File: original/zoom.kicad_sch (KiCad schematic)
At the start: 161 parts, among them U10 1NB4-5040, U11 1NB4-5040, U12 1NB4-5040, U14 1821-4731, U2 LM2991, U7 LT1086-CM, U77 74LVC08, U78 74LVC08, U8 1NB4-5040, U9 1NB4-5040

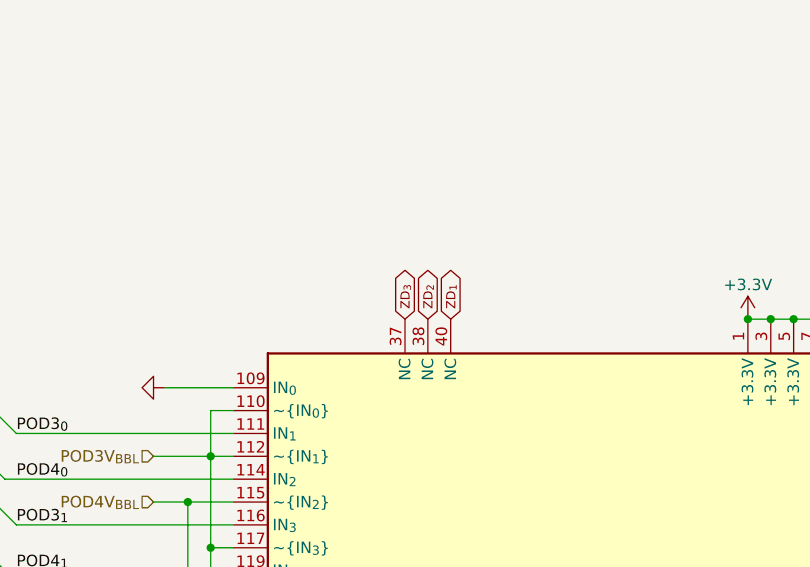
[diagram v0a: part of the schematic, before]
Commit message: fix original version ECL routing to ASICs
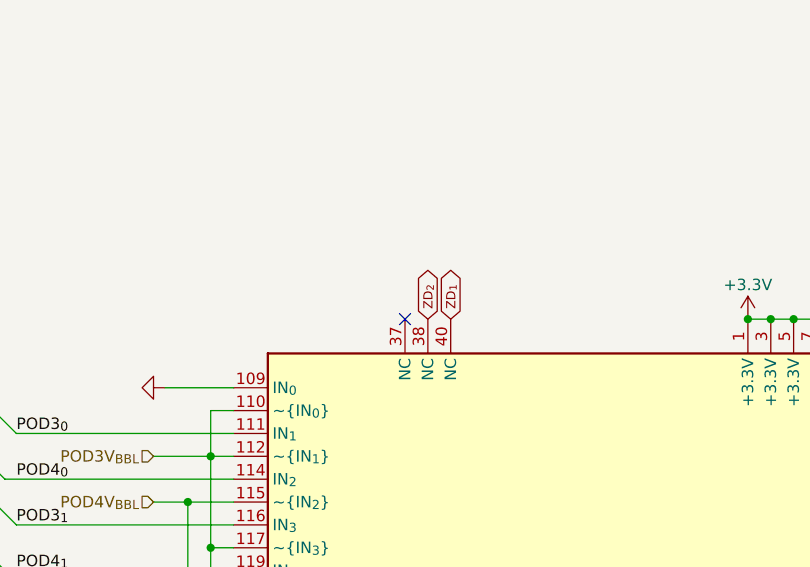
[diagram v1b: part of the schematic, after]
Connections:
- net ZD_{3}: no longer U12.37 (NC)
- no-connect marks 31 -> 32
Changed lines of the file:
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@@
 	)
 	(no_connect
+		(at 214.63 81.28)
+	)
+	(no_connect
 		(at 318.77 219.71)
 	)
@@
 			(effects
 				(font
-					(size 1.27 1.27)
-				)
-				(justify left)
-				(hide yes)
-			)
-		)
-	)
-	(global_label "ZD_{3}"
-		(shape bidirectional)
-		(at 214.63 81.28 90)
-		(fields_autoplaced yes)
-		(effects
-			(font
-				(size 1.016 1.016)
-			)
-			(justify left)
-		)
-		(property "Intersheetrefs" "${INTERSHEET_REFS}"
-			(at 214.63 75.2048 90)
-			(effects
-				(font

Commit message: clean up routing & add test points on original design
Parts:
- removed C1081, C1085, C1291, C1305, C1321, C1327: 100p, fp:C0603, symbol Device:C_Small
- added TP1087, TP1088, TP121, TP122, TP123, TP124, TP125, TP126, TP127, TP128, TP370, TP547, TP548, TP549, TP554, TP613, TP652, TP653, TP654, TP655, TP656, TP657, TP658, TP659, TP661, TP78, TP784, TP79, TP80, TP816, TP817, TP818, TP819, TP820, TP821, TP822, TP823, TP824, TP825, TP826, TP827, TP828, TP830, TP832, TP833, TP834, TP835, TP836, TP856, TP857, TP858, TP859, TP860, TP861, TP862, TP863, TP864, TP867, TP868, TP869, TP870, TP871, TP872, TP874, TP880, TP881, TP882, TP883, TP884, TP885, TP886, TP887, TP888, TP889, TP890, TP891, TP892, TP893, TP894, TP895, TP896: ~, fp:TestPoint, symbol 16717a:TestPoint_Small
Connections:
- net +3.3V: now also TP816.1, TP818.1, TP819.1, TP821.1, TP823.1, TP825.1, TP826.1, TP828.1, TP830.1, TP833.1, TP834.1, TP856.1, TP857.1, TP880.1, TP896.1
- net +3.3VP: now also TP1087.1, TP1088.1, TP549.1; no longer U2.2 (~{ON}/OFF)
- net -1.7V: now also TP79.1
- net -3.3V: now also TP548.1
- net CLKA_{0}-: now also TP653.1
- net CLKA_{1}-: now also TP655.1
- net CLKA_{2}-: now also TP657.1
- net CLKA_{3}-: now also TP659.1
- net CLKA_{4}+: now also TP661.1
- net CLKB_{0}+: now also TP652.1
- net CLKB_{1}+: now also TP654.1
- net CLKB_{2}+: now also TP656.1
- net CLKB_{3}+: now also TP658.1
- net GND: now also TP554.1, TP613.1, TP78.1, TP784.1, TP80.1, TP817.1, TP820.1, TP822.1, TP824.1, TP827.1, TP832.1, TP835.1, TP836.1, TP859.1, TP860.1, TP861.1, TP862.1, TP863.1, TP864.1, TP874.1; no longer U78.10, U78.12, U78.13, U78.4, U78.5, U78.9
- net POD1V_{BB}_{H}: now also TP867.1
- net POD1_{4}: now also TP370.1
- net POD2V_{BB}_{H}: now also TP872.1
- net POD2V_{BB}_{L}: now also TP868.1
- net POD3V_{BB}_{H}: now also TP869.1
- net POD4V_{BB}_{H}: now also TP871.1
- net POD4V_{BB}_{L}: now also TP870.1
- net ZD_{0}: now also TP121.1
- net ZD_{1}: now also TP122.1
- net ZD_{2}: now also TP123.1
- net ZD_{3}: now also TP124.1
- net ZD_{4}: now also TP125.1
- net ZD_{5}: now also TP126.1
- net ZD_{6}: now also TP127.1
- net ZD_{7}: now also TP128.1
- net at C1336.1, R1260.2, R1265.1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: now also TP858.1
- net at RP1.16, RP14.1, U14.5 (CTRL3): now also TP883.1
- net at RP1.15, RP14.2, U14.4 (CTRL2): now also TP881.1
- net at RP1.14, RP14.3, U14.22 (CTRL6): now also TP884.1
- net at RP1.13, RP14.4, U14.21 (CTRL5): now also TP885.1
- net at RP1.12, RP14.5, U14.20 (CTRL4): now also TP886.1
- net at RP1.11, RP14.6, U14.94 (CTRL1): now also TP887.1
- net at RP1.10, RP14.7, U14.6 (CTRL0): now also TP888.1
- net at RP15.1, RP2.16, U14.17 (D_{0}): now also TP895.1
- net at RP15.2, RP2.15, U14.16 (D_{1}): now also TP894.1
- net at RP15.3, RP2.14, U14.15 (D_{2}): now also TP893.1
- net at RP15.4, RP2.13, U14.14 (D_{3}): now also TP892.1
- net at RP15.5, RP2.12, U14.12 (D_{4}): now also TP891.1
- net at RP15.6, RP2.11, U14.11 (D_{5}): now also TP890.1
- net at RP15.7, RP2.10, U14.10 (D_{6}): now also TP889.1
- net at RP15.8, RP2.9, U14.9 (D_{7}): now also TP882.1
- net at R1283.1, R1288.1, U2.1 (ADJ): now also TP547.1
- no-connect marks 32 -> 39
